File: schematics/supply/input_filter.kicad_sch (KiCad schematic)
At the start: 47 parts, among them J5 AS-230UL with fuse 9A, K1 SRD-12VDC-SL-C, U1 ICE2PCS01, U2 TL331, X1 B32922-C3104-K, 0.1 uF, X2 B32922-C3104-K, 0.1 uF, Y1 B32022A3223M000, Y2 B32022A3223M000, Y3 B32022A3223M000

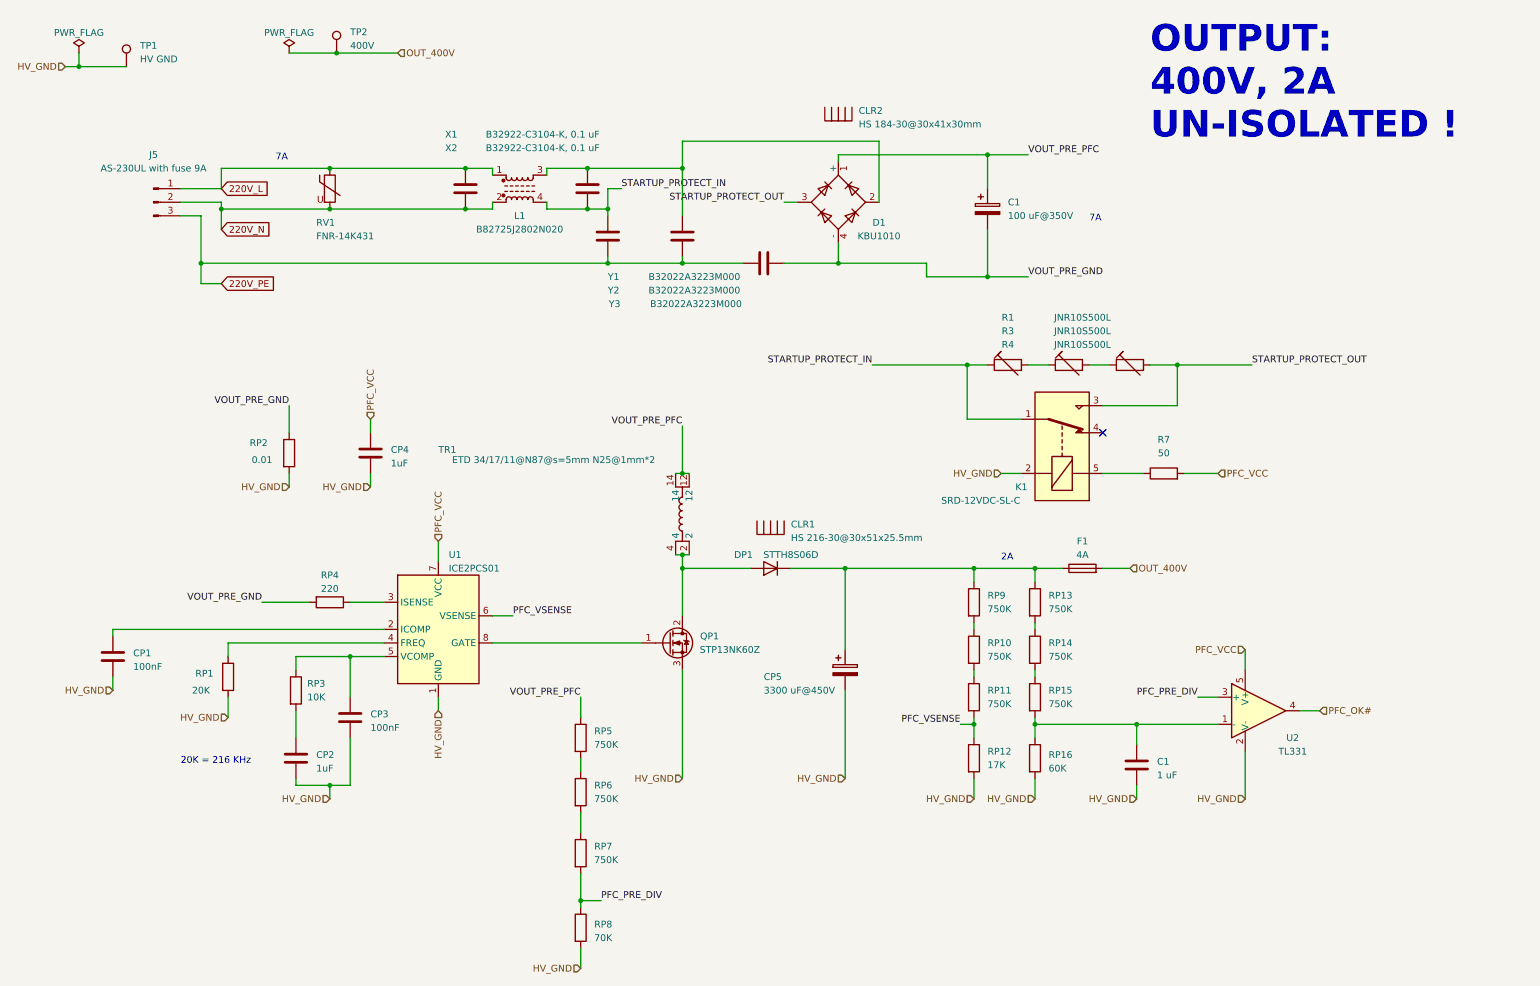
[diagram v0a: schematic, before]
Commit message: prepare to replace ina228 to attiny16+ina169(?). ina228 is an intresting chip, but its too expensive and Im not sure I can buy it on ali
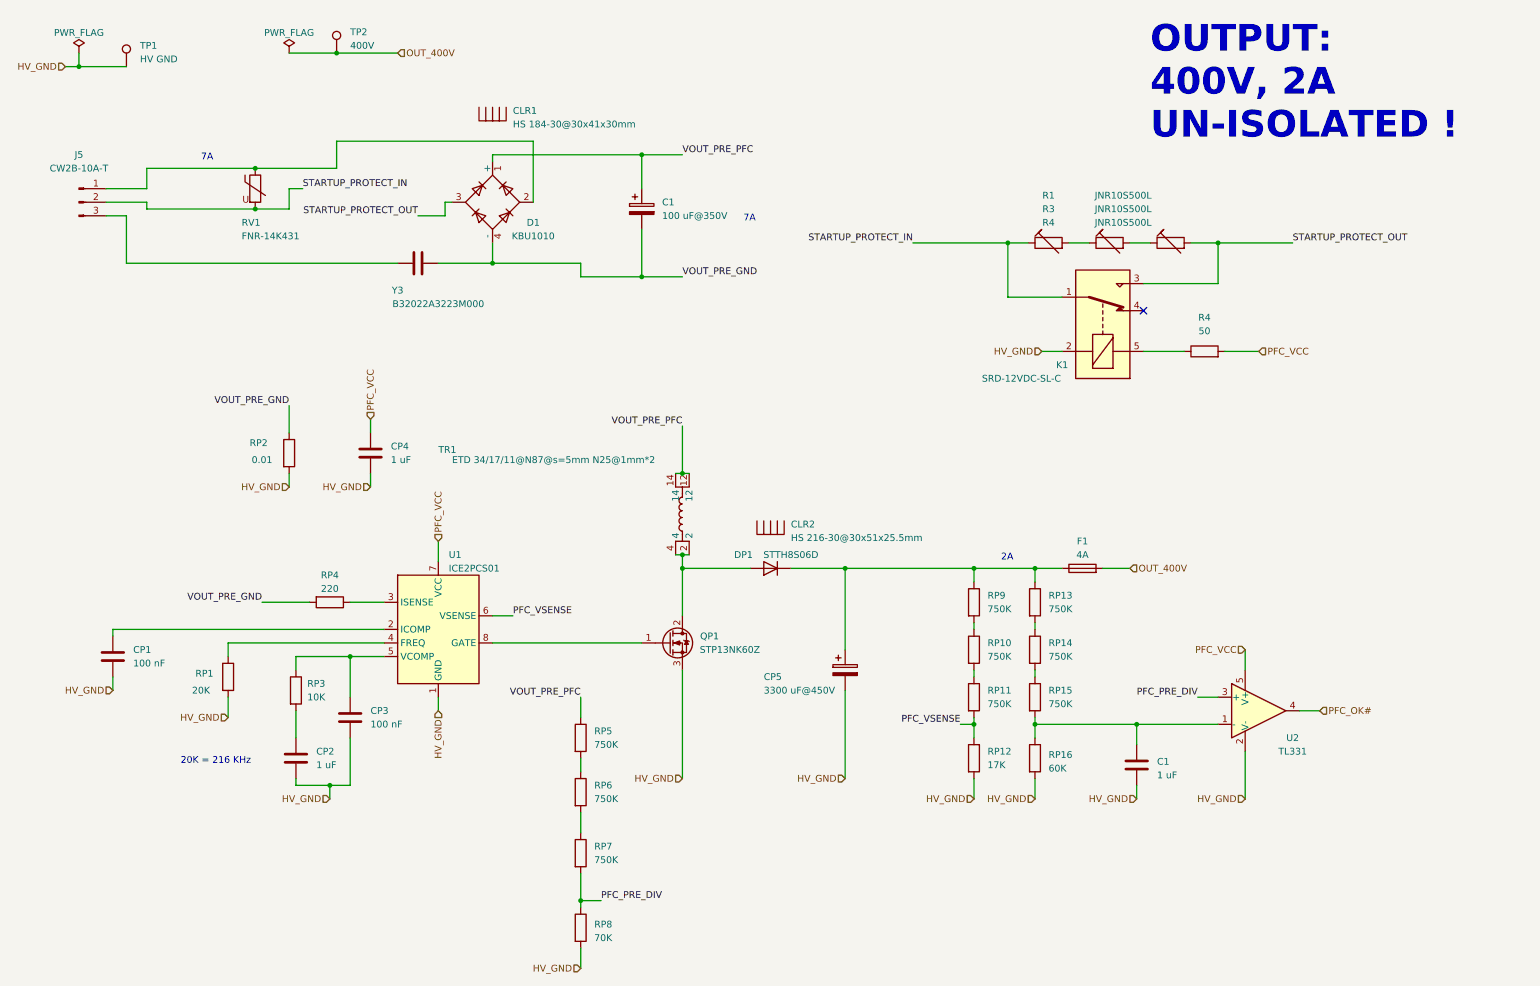
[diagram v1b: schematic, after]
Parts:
- removed L1: B82725J2802N020, Library:B82725j, symbol Device:L_Ferrite_Coupled_1324
- removed X1, X2: B32922-C3104-K, 0.1 uF, Capacitor_THT:C_Rect_L18.0mm_W5.0mm_P15.00mm_FKS3_FKP3, symbol Device:C
- removed Y1, Y2: B32022A3223M000, Capacitor_THT:C_Rect_L18.0mm_W6.0mm_P15.00mm_FKS3_FKP3, symbol Device:C
- CP1, CP3: value 100nF -> 100 nF
- CP2, CP4: value 1uF -> 1 uF
- J5: value AS-230UL with fuse 9A -> CW2B-10A-T
- renumbered CLR2 to CLR1, CLR1 to CLR2, R7 to R4
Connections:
- net 220V_L is gone; now on an unnamed net: J5.1 (Pin_1), RV1.1
- net 220V_N is gone; now on net STARTUP_PROTECT_IN: J5.2 (Pin_2), RV1.2
- net 220V_PE: no longer names the net of J5.3 (Pin_3), Y3.1
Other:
- moved on the sheet: C1, CLR1, D1, J5, K1, R1, R3, R4, RV1, Y3

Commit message: little changes in schematics
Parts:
- RP2: footprint Resistor_SMD:R_1206_3216Metric -> Resistor_SMD:R_2512_6332Metric
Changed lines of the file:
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@@
       (effects (font (size 1.27 1.27)))
     )
-    (property "Footprint" "Resistor_SMD:R_1206_3216Metric" (at 64.262 93.98 90)
+    (property "Footprint" "Resistor_SMD:R_2512_6332Metric" (at 64.262 93.98 90)
       (effects (font (size 1.27 1.27)) hide)
     )

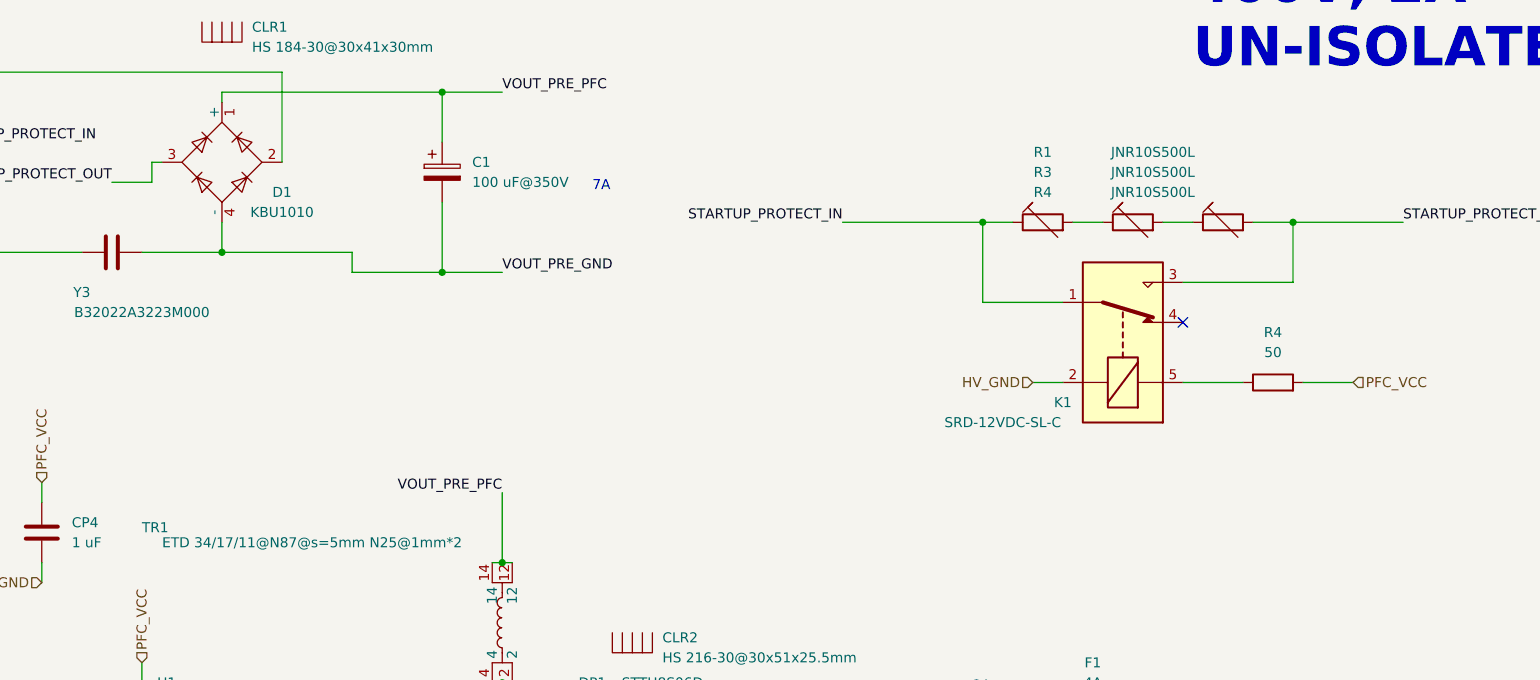
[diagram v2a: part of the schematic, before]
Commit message: Fixed problem with 20V on one leg of comparator
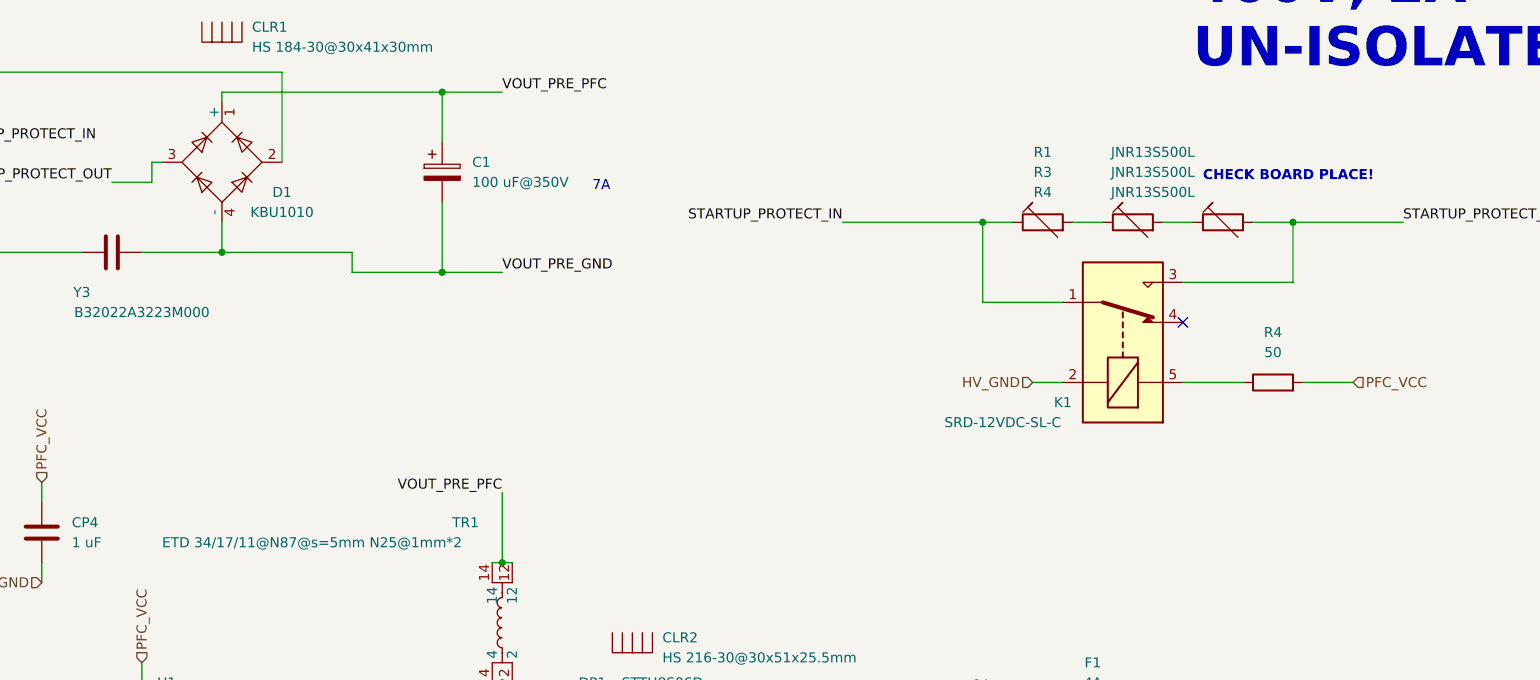
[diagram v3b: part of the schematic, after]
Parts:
- R1, R3, R4: value JNR10S500L -> JNR13S500L
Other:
- note added: "CHECK BOARD PLACE!"
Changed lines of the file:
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@@
     (effects (font (size 1.27 1.27)) (justify left bottom))
+  )
+  (text "CHECK BOARD PLACE!" (at 228.6 49.53 0)
+    (effects (font (size 1.27 1.27) (thickness 0.254) bold) (justify left bottom))
   )
   (text "OUTPUT:\n400V, 2A\nUN-ISOLATED !" (at 227.33 35.56 0)
@@
   (symbol (lib_id "My_Library:TR_1x2-8+8") (at 139.7 105.41 270) (unit 1)
     (in_bom yes) (on_board yes) (dnp no)
-    (property "Reference" "TR1" (at 93.98 93.345 90)
+    (property "Reference" "TR1" (at 133.35 92.71 90)
       (effects (font (size 1.27 1.27)) (justify left))
     )
@@
       (effects (font (size 1.27 1.27)))
     )
-    (property "Value" "JNR10S500L" (at 222.25 45.72 90)
+    (property "Value" "JNR13S500L" (at 222.25 45.72 90)
       (effects (font (size 1.27 1.27)))
     )
@@
       (effects (font (size 1.27 1.27)))
     )
-    (property "Value" "JNR10S500L" (at 222.25 48.26 90)
+    (property "Value" "JNR13S500L" (at 222.25 48.26 90)
       (effects (font (size 1.27 1.27)))
     )
@@
       (effects (font (size 1.27 1.27)))
     )
-    (property "Value" "JNR10S500L" (at 222.25 50.8 90)
-      (effects (font (size 1.27 1.27)))
-    )
+    (property "Value" "JNR13S500L" (at 222.25 50.8 90)
+      (effects (font (size 1.27 1.27)))
+    )

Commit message: Some changes in board - Im preparing it to production
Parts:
- F1: value 4A -> 1808, 4A
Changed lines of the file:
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@@
       (effects (font (size 1.27 1.27)))
     )
-    (property "Value" "4A" (at 214.63 113.03 90)
+    (property "Value" "1808, 4A" (at 214.63 113.03 90)
       (effects (font (size 1.27 1.27)))
     )

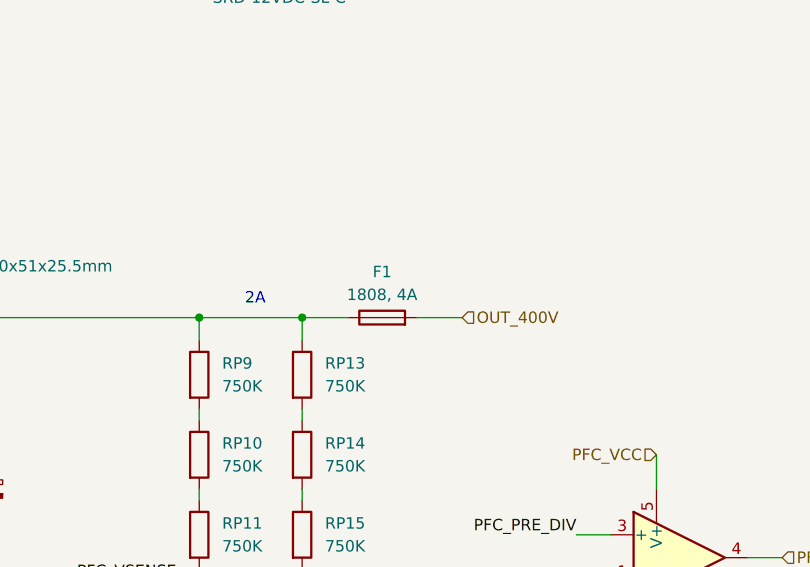
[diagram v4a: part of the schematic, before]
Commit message: Changed fuse on 400V line
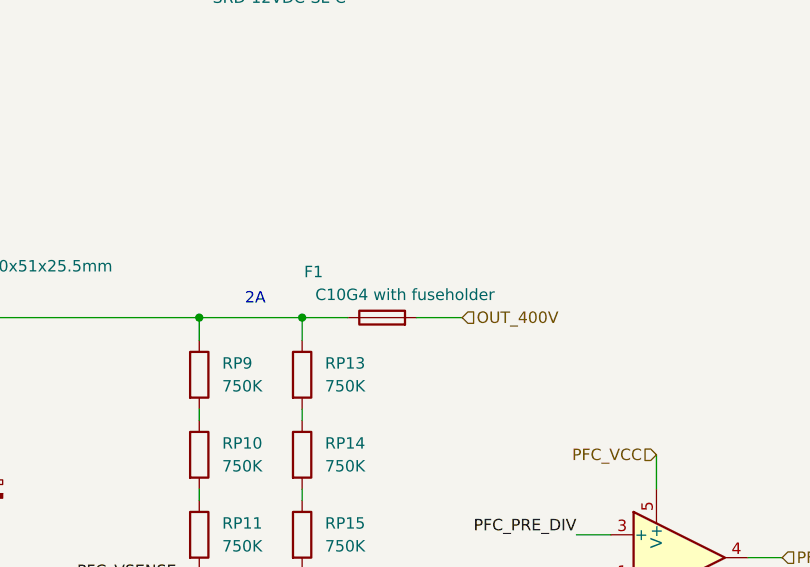
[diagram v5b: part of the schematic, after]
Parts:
- F1: value 1808, 4A -> C10G4 with fuseholder; footprint Library:FuseHolder1808 -> Connector_Wire:SolderWire-1.5sqmm_1x02_P6mm_D1.7mm_OD3mm
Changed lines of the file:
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@@
   )
   (symbol (lib_id "Device:Fuse") (at 214.63 115.57 90) (unit 1)
-    (in_bom yes) (on_board yes) (dnp no) (fields_autoplaced)
-    (property "Reference" "F1" (at 214.63 110.49 90)
+    (in_bom yes) (on_board yes) (dnp no)
+    (property "Reference" "F1" (at 207.01 110.49 90)
       (effects (font (size 1.27 1.27)))
     )
-    (property "Value" "1808, 4A" (at 214.63 113.03 90)
+    (property "Value" "C10G4 with fuseholder" (at 217.17 113.03 90)
       (effects (font (size 1.27 1.27)))
     )
-    (property "Footprint" "Library:FuseHolder1808" (at 214.63 117.348 90)
+    (property "Footprint" "Connector_Wire:SolderWire-1.5sqmm_1x02_P6mm_D1.7mm_OD3mm" (at 214.63 117.348 90)
       (effects (font (size 1.27 1.27)) hide)
     )
